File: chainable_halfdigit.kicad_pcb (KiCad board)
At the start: 2 copper layers, 100 x 100 mm, 61 parts, among them J1 Conn_01x03, J2 Conn_01x03, U1 arduino_nano

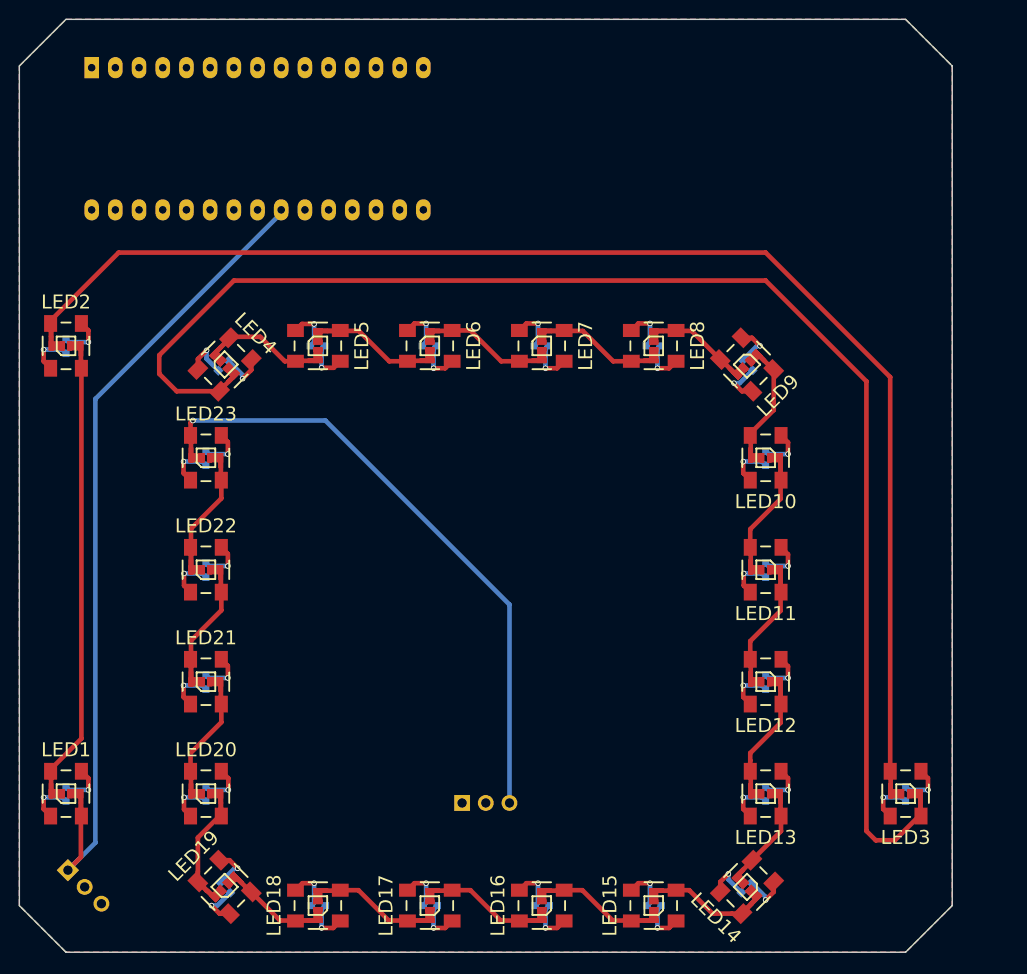
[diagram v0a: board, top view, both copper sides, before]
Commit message: Placed mounting holes, updated WS2812B footprint with PIN1 marker.
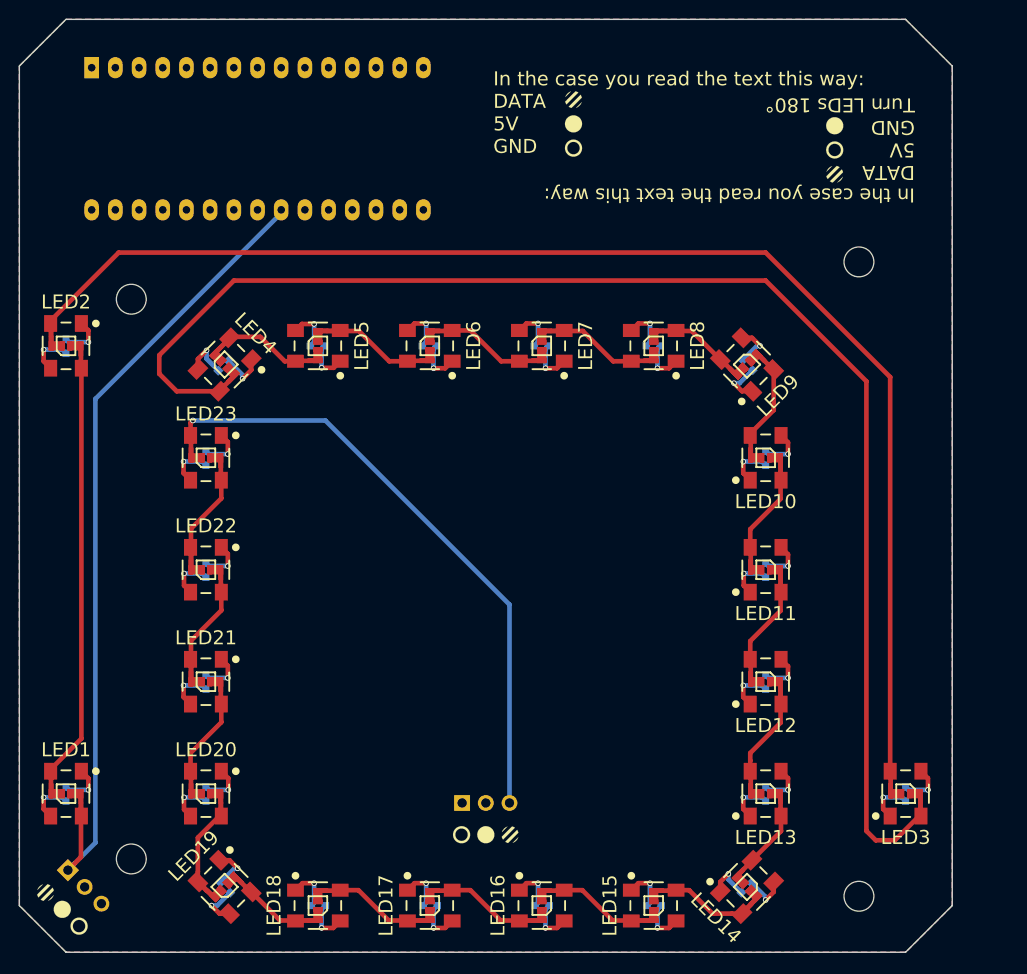
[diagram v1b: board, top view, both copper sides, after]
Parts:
- added G***: LOGO, lib_fp:legend_item_round_stripe, F.Cu at (149.4, 58.6)
- added G***: LOGO, lib_fp:legend_item_round_circled, F.Cu at (96.4, 147.2)
- added G***: LOGO, lib_fp:legend_item_round_plain, F.Cu at (94.6, 145.4)
- added G***: LOGO, lib_fp:legend_item_round_stripe, F.Cu at (92.8, 143.6)
- added G***: LOGO, lib_fp:legend_item_round_circled, F.Cu at (149.4, 63.8)
- added G***: LOGO, lib_fp:legend_item_round_plain, F.Cu at (149.4, 61.2)
- added G***: LOGO, lib_fp:legend_item_round_plain, F.Cu at (177.4, 61.4)
- added G***: LOGO, lib_fp:legend_item_round_stripe, F.Cu at (177.4, 66.6)
- added G***: LOGO, lib_fp:legend_item_round_circled, F.Cu at (177.4, 64.0)
- added G***: LOGO, lib_fp:legend_item_round_stripe, F.Cu at (142.6, 137.4)
- added G***: LOGO, lib_fp:legend_item_round_plain, F.Cu at (140.0, 137.4)
- added G***: LOGO, lib_fp:legend_item_round_circled, F.Cu at (137.4, 137.4)
- added REF**: MountingHole_3.2mm_M3, Mounting_Holes:MountingHole_3.2mm_M3, F.Cu at (180.0, 76.0)
- added REF**: MountingHole_3.2mm_M3, Mounting_Holes:MountingHole_3.2mm_M3, F.Cu at (180.0, 144.0)
- added REF**: MountingHole_3.2mm_M3, Mounting_Holes:MountingHole_3.2mm_M3, F.Cu at (102.0, 140.0)
- added REF**: MountingHole_3.2mm_M3, Mounting_Holes:MountingHole_3.2mm_M3, F.Cu at (102.0, 80.0)
- moved G*** 2.80 mm to (177.4, 61.6)
- moved G*** 2.60 mm to (149.4, 64.4)
- moved G*** 2.60 mm to (149.4, 67.0)
- moved G*** 2.40 mm to (177.4, 64.2)
- moved G*** 0.20 mm to (177.4, 59.0)
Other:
- board text added: "In the case you read the text this way: DATA 5V GND"
- board text added: "In the case you read the text this way: DATA 5V GND Turn LEDs 180°"
- board text removed: "In the case you read the text this way: 5V DATA GND"
- board text removed: "In the case you read the text this way: 5V DATA GND Turn LEDs 180°"

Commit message: Changed DATA_IN in arduino nano from D4 to D3. Moved some components.
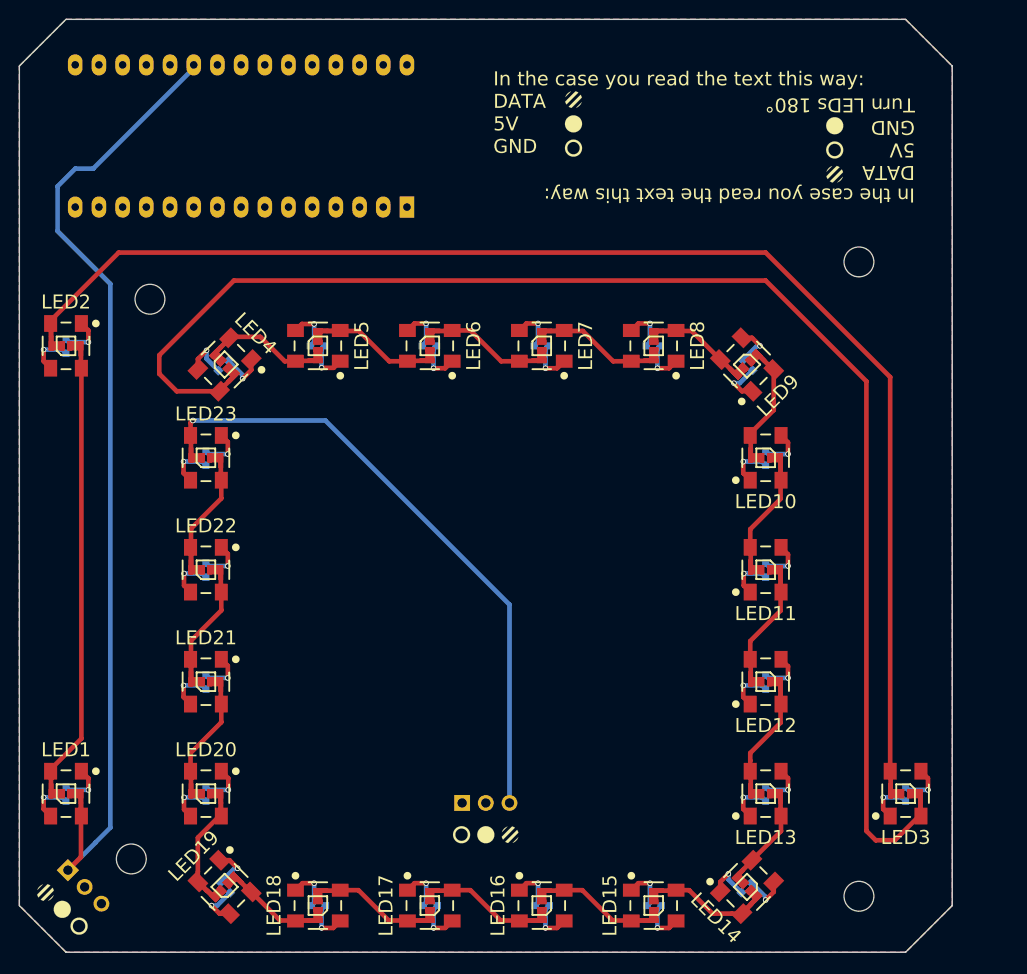
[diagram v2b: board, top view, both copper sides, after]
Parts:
- moved U1 4.31 mm to (112.5, 62.5), turned to 180 degrees
- moved REF** 2.00 mm to (104.0, 80.0)
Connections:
- U1 pad 21: Net-(U1-Pad21) -> DATA_IN
- U1 pad 22: DATA_IN -> Net-(U1-Pad22)
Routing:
- net DATA_IN: track 88.0 -> 105.5 mm

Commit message: Added a mounting hole, edited some tracks
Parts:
- added REF**: MountingHole_3.2mm_M3, Mounting_Holes:MountingHole_3.2mm_M3, F.Cu at (106.0, 61.0)
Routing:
- net DATA_IN: track 105.5 -> 115.2 mm, vias 0 -> 6
- net Net-(LED2-Pad2): track 142.5 -> 147.1 mm, vias 0 -> 2

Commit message: Added info and logo
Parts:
- added G***: LOGO, lib_fp:logo_igrebot, F.Cu at (140.0, 112.5)
- added REF***: OSHW-Logo2_14.6x12mm_SilkScreen, Symbols:OSHW-Logo2_14.6x12mm_SilkScreen, F.Cu at (140.0, 100.0)
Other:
- board text added: "Yannick Chiron Chainable Half-digit V1 - 12/2017"
